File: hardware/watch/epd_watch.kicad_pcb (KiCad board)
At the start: 4 copper layers, 34.5 x 39 mm, 63 parts, among them P1 FPC, Q1 Si1308EDL, Q2 AO3401A, Q3 Si1308EDL, SW1 BTN_UP, SW2 BTN_MIDDLE, SW3 BTN_DOWN, U1 nRF52832-QFxx, U2 XC6206PxxxMR, U3 TP4057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

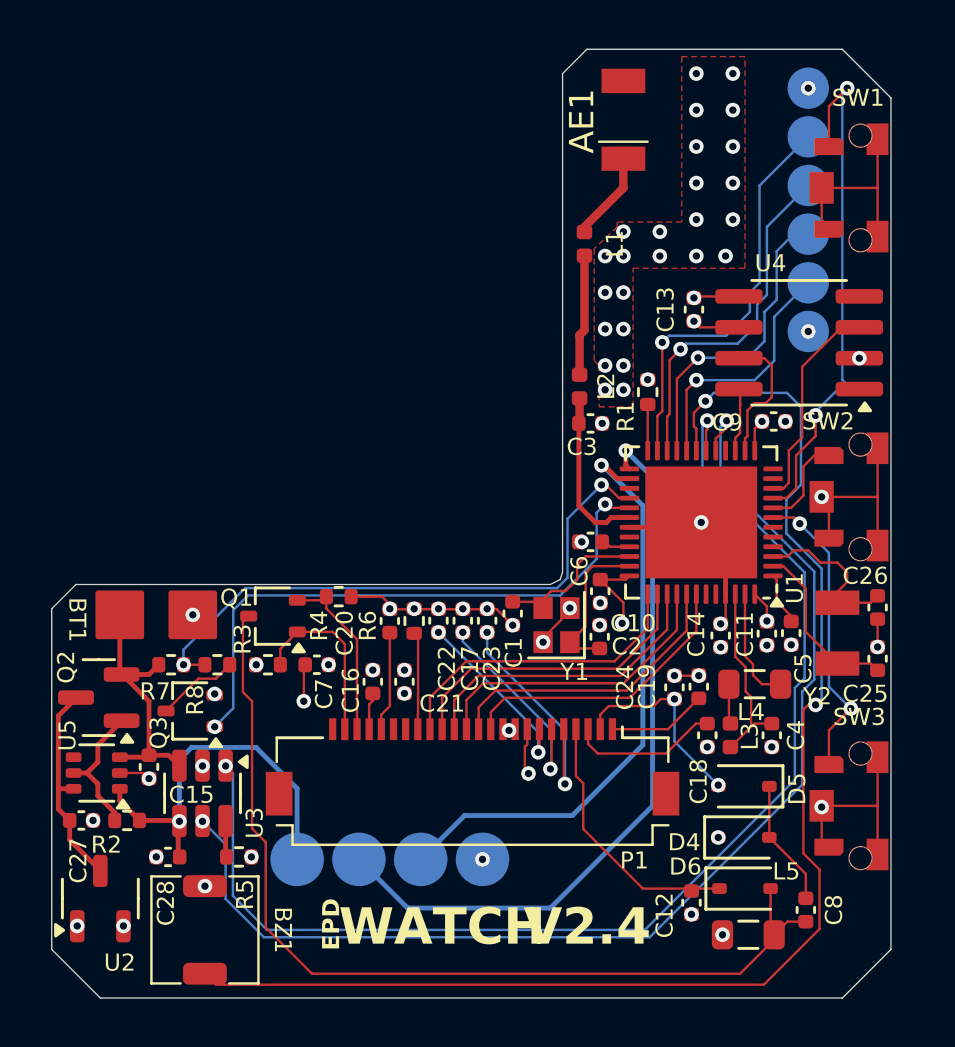
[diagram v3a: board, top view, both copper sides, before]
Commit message: updated code to work for board
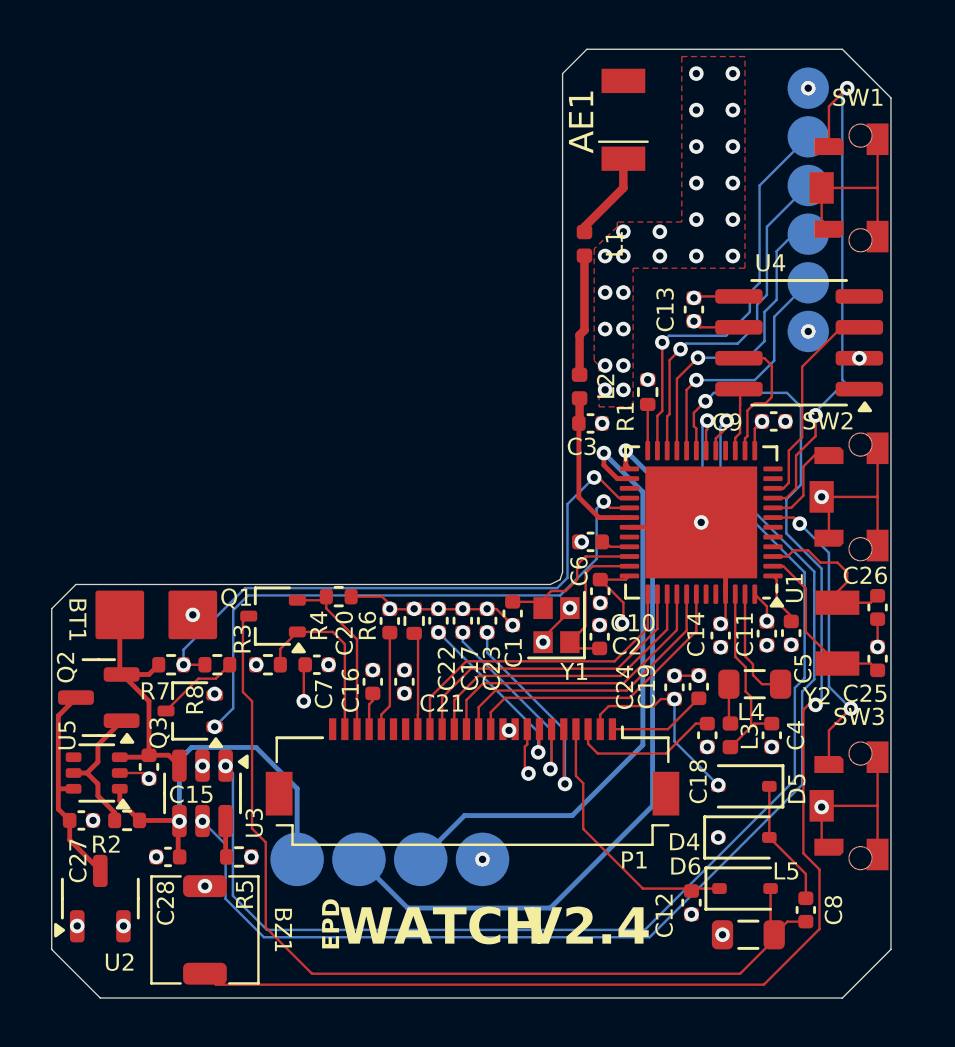
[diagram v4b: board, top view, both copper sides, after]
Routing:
- net SWDIO: track 24.7 -> 25.5 mm
- net BAT_LVL: track 24.3 -> 25.1 mm
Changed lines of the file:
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@@
 	)
 	(via
-		(at 159.2 93.5)
+		(at 159.5 93.5)
 		(size 0.6)
 		(drill 0.3)
@@
 	)
 	(segment
-		(start 153.2 100.35)
+		(start 153.17 103.423412)
 		(end 153.17 100.38)
-		(width 0.3493)
-		(layer "F.Cu")
-		(net 23)
-	)
-	(segment
-		(start 154.5 104.25)
-		(end 154.3 104.45)
 		(width 0.2)
 		(layer "F.Cu")
@@
 	)
 	(segment
-		(start 155.25 104.25)
-		(end 154.5 104.25)
-		(width 0.2)
+		(start 153.2 100.35)
+		(end 153.17 100.38)
+		(width 0.3493)
 		(layer "F.Cu")
 		(net 23)
 	)
 	(segment
-		(start 153.17 103.77)
-		(end 153.17 100.38)
+		(start 153.996588 104.25)
+		(end 153.17 103.423412)
 		(width 0.2)
 		(layer "F.Cu")
@@
 	)
 	(segment
-		(start 153.85 104.45)
-		(end 153.17 103.77)
+		(start 155.25 104.25)
+		(end 153.996588 104.25)
 		(width 0.2)
 		(layer "F.Cu")
@@
 	)
 	(segment
-		(start 154.3 104.45)
-		(end 153.85 104.45)
-		(width 0.2)
-		(layer "F.Cu")
-		(net 23)
-	)
-	(segment
 		(start 152.63 107.27)
 		(end 153.1 106.8)
@@
 	)
 	(segment
-		(start 155.25 102.65)
+		(start 154.2 102.1)
 		(end 154.75 102.65)
 		(width 0.2)
@@
 	)
 	(segment
-		(start 154.75 102.65)
+		(start 154.2 101.6)
 		(end 154.2 102.1)
 		(width 0.2)
@@
 	)
 	(segment
-		(start 154.2 102.1)
-		(end 154.1 102.1)
+		(start 154.75 102.65)
+		(end 155.25 102.65)
 		(width 0.2)
 		(layer "F.Cu")
 		(net 27)
 	)
-	(segment
-		(start 154.2 102.2)
-		(end 154.222415 102.2)
-		(width 0.1)
-		(layer "F.Cu")
-		(net 27)
-	)
 	(via
-		(at 154.1 102.1)
+		(at 154.2 101.6)
 		(size 0.6)
 		(drill 0.3)
@@
 	)
 	(segment
-		(start 155.8 103.756234)
-		(end 154.143766 102.1)
-		(width 0.2)
-		(layer "B.Cu")
-		(net 27)
-	)
-	(segment
-		(start 152.9 116.5)
+		(start 155.8 103.2)
 		(end 155.8 113.6)
 		(width 0.2)
@@
 	)
 	(segment
-		(start 154.143766 102.1)
-		(end 154.1 102.1)
+		(start 155.8 113.6)
+		(end 152.9 116.5)
 		(width 0.2)
 		(layer "B.Cu")
@@
 	(segment
 		(start 148.47 116.5)
-		(end 152.9 116.5)
+		(end 146.67 118.3)
 		(width 0.2)
 		(layer "B.Cu")
@@
 	)
 	(segment
-		(start 146.67 118.3)
-		(end 148.47 116.5)
+		(start 154.2 101.6)
+		(end 155.8 103.2)
 		(width 0.2)
 		(layer "B.Cu")
@@
 	)
 	(segment
-		(start 155.8 113.6)
-		(end 155.8 103.756234)
+		(start 152.9 116.5)
+		(end 148.47 116.5)
 		(width 0.2)
 		(layer "B.Cu")
@@
 	)
 	(segment
-		(start 146.13 120.3)
-		(end 152 120.3)
+		(start 155.1 101.5)
+		(end 156.2 102.6)
 		(width 0.2)
 		(layer "B.Cu")
@@
 	)
 	(segment
-		(start 144.13 118.3)
-		(end 146.13 120.3)
+		(start 156.2 102.6)
+		(end 156.2 116.1)
 		(width 0.2)
 		(layer "B.Cu")
@@
 	)
 	(segment
-		(start 156.2 102.6)
-		(end 155.1 101.5)
+		(start 146.13 120.3)
+		(end 144.13 118.3)
 		(width 0.2)
 		(layer "B.Cu")
@@
 	(segment
 		(start 152 120.3)
-		(end 156.2 116.1)
+		(end 146.13 120.3)
 		(width 0.2)
 		(layer "B.Cu")
@@
 	(segment
 		(start 156.2 116.1)
-		(end 156.2 102.6)
+		(end 152 120.3)
 		(width 0.2)
 		(layer "B.Cu")
@@
 	)
 	(segment
-		(start 154.25 103.7)
-		(end 154.4 103.85)
+		(start 155.25 103.85)
+		(end 154.446531 103.85)
 		(width 0.1)
 		(layer "F.Cu")
@@
 	)
 	(segment
-		(start 154.4 103.85)
-		(end 155.25 103.85)
+		(start 154.446531 103.85)
+		(end 154.190245 103.593714)
 		(width 0.1)
 		(layer "F.Cu")
@@
 	)
 	(via
-		(at 154.25 103.7)
+		(at 154.190245 103.593714)
 		(size 0.6)
 		(drill 0.3)
@@
 	)
 	(segment
-		(start 138.2 112.85)
-		(end 138.962132 112.087868)
+		(start 138.962132 108.062132)
+		(end 139.574264 107.45)
 		(width 0.1)
 		(layer "B.Cu")
@@
 	)
 	(segment
-		(start 138.962132 108.062132)
-		(end 139.574264 107.45)
+		(start 138.962132 112.087868)
+		(end 138.962132 108.062132)
 		(width 0.1)
 		(layer "B.Cu")
@@
 	)
 	(segment
-		(start 152.403296 107.45)
-		(end 153.9 105.953296)
+		(start 139.574264 107.45)
+		(end 152.403296 107.45)
 		(width 0.1)
 		(layer "B.Cu")
@@
 	)
 	(segment
-		(start 138.962132 112.087868)
-		(end 138.962132 108.062132)
+		(start 152.403296 107.45)
+		(end 153.9 105.953296)
 		(width 0.1)
 		(layer "B.Cu")
@@
 	)
 	(segment
-		(start 153.9 105.953296)
-		(end 153.9 104.05)
+		(start 138.2 112.85)
+		(end 138.962132 112.087868)
 		(width 0.1)
 		(layer "B.Cu")
@@
 	)
 	(segment
-		(start 139.574264 107.45)
-		(end 152.403296 107.45)
+		(start 153.9 105.953296)
+		(end 153.9 103.883959)
 		(width 0.1)
 		(layer "B.Cu")
@@
 	)
 	(segment
-		(start 153.9 104.05)
-		(end 154.25 103.7)
+		(start 153.9 103.883959)
+		(end 154.190245 103.593714)
 		(width 0.1)
 		(layer "B.Cu")
@@
 	)
 	(segment
-		(start 154.82435 103.45)
-		(end 155.25 103.45)
+		(start 153.976732 102.602382)
+		(end 154.82435 103.45)
 		(width 0.1)
 		(layer "F.Cu")
@@
 	)
 	(segment
-		(start 154.280527 102.906177)
-		(end 154.82435 103.45)
+		(start 153.797618 102.602382)
+		(end 153.978145 102.602382)
 		(width 0.1)
 		(layer "F.Cu")
@@
 	)
 	(segment
-		(start 154.1 102.906177)
-		(end 154.1 102.9)
+		(start 153.797618 102.602382)
+		(end 153.976732 102.602382)
 		(width 0.1)
 		(layer "F.Cu")
@@
 	)
 	(segment
-		(start 154.1 102.906177)
-		(end 154.280527 102.906177)
+		(start 154.82435 103.45)
+		(end 155.25 103.45)
 		(width 0.1)
 		(layer "F.Cu")
@@
 	)
 	(via
-		(at 154.1 102.906177)
+		(at 153.797618 102.602382)
 		(size 0.6)
 		(drill 0.3)
@@
 	)
 	(segment
-		(start 152.279032 107.15)
-		(end 152.7 106.729032)
+		(start 152.7 106.729032)
+		(end 152.7 103.7)
 		(width 0.1)
 		(layer "B.Cu")
@@
 	)
 	(segment
-		(start 152.7 104.306177)
-		(end 154.1 102.906177)
+		(start 152.7 103.7)
+		(end 153.797618 102.602382)
 		(width 0.1)
 		(layer "B.Cu")
@@
 	)
 	(segment
-		(start 152.7 106.729032)
-		(end 152.7 104.306177)
+		(start 152.279032 107.15)
+		(end 152.7 106.729032)
 		(width 0.1)
 		(layer "B.Cu")
